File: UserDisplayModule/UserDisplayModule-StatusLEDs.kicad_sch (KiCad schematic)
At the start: 15 parts, among them U1 74HC595

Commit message: doubled LEDs + started PCB
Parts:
- removed D20: SYSTEM FAIL, symbol Device:LED
- removed D21: COL2, symbol Device:LED
- removed D23: COL1, symbol Device:LED
- removed D4: SYSTEM WARN, symbol Device:LED
- added D10, D43, D45: BAT3, LED_SMD:LED_0805_2012Metric, symbol Device:LED
- added D2: MAINS, LED_SMD:LED_0805_2012Metric, symbol Device:LED
- added D42: COL2, LED_SMD:LED_0805_2012Metric, symbol Device:LED
- added D44: COL1, LED_SMD:LED_0805_2012Metric, symbol Device:LED
- added D5: BATTERY, LED_SMD:LED_0805_2012Metric, symbol Device:LED
- added D6: BAT7, LED_SMD:LED_0805_2012Metric, symbol Device:LED
- added D7: SYS WARN, LED_SMD:LED_0805_2012Metric, symbol Device:LED
- added D8: BAT5, LED_SMD:LED_0805_2012Metric, symbol Device:LED
- added D9: SYS FAIL, LED_SMD:LED_0805_2012Metric, symbol Device:LED
- D1: footprint (none) -> LED_SMD:LED_0805_2012Metric
- D3: renamed from D2; footprint (none) -> LED_SMD:LED_0805_2012Metric
- D4: renamed from D3; footprint (none) -> LED_SMD:LED_0805_2012Metric
- R1, R2, R20, R21, R23, R3, R4: footprint (none) -> Resistor_SMD:R_0805_2012Metric
- U1: footprint (none) -> ImportedFootprints:CD74HC595E
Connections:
- net GND: now also D10.1 (K), D2.1 (K), D43.1 (K), D45.1 (K), D6.1 (K), D8.1 (K); no longer D1.1 (K), D3.1 (K)
- net at R21.2: now also D42.2 (A)
- net at R23.2: now also D44.2 (A)
- net at R3.2: now also D5.2 (A); no longer D4.2 (A)
- net at R20.2: now also D9.2 (A)
- net at R4.2: now also D7.2 (A)
- new net: D42.1 (K), D43.2 (A)
- new net: D44.1 (K), D45.2 (A)
- new net: D7.1 (K), D8.2 (A)
- new net: D1.1 (K), D2.2 (A)
- new net: D3.1 (K), D4.2 (A)
- new net: D10.2 (A), D9.1 (K)
- new net: D5.1 (K), D6.2 (A)
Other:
- moved on the sheet: D4, R20, R21, R23

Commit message: started routing (help)
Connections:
- net at R23.1: now also U1.6 (QG); no longer U1.1 (QB)
- net at R1.1: now also U1.5 (QF); no longer U1.7 (QH)
- net at R3.1: now also U1.3 (QD); no longer U1.5 (QF)
- net at R21.1: now also U1.7 (QH); no longer U1.2 (QC)
- net at R20.1: now also U1.1 (QB); no longer U1.3 (QD)
- net at R2.1: now also U1.4 (QE); no longer U1.6 (QG)
- net at R4.1: now also U1.2 (QC); no longer U1.4 (QE)
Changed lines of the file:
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@@
-	(wire
-		(pts
-			(xy 100.33 83.82) (xy 157.48 83.82)
-		)
-		(stroke
-			(width 0)
-			(type default)
-		)
-	)
 	(wire
 		(pts
@@
 	(wire
 		(pts
+			(xy 100.33 88.9) (xy 200.66 88.9)
+		)
+		(stroke
+			(width 0)
+			(type default)
+		)
+	)
+	(wire
+		(pts
+			(xy 100.33 78.74) (xy 157.48 78.74)
+		)
+		(stroke
+			(width 0)
+			(type default)
+		)
+	)
+	(wire
+		(pts
 			(xy 119.38 119.38) (xy 132.08 119.38)
 		)
@@
 	(wire
 		(pts
+			(xy 100.33 76.2) (xy 170.18 76.2)
+		)
+		(stroke
+			(width 0)
+			(type default)
+		)
+	)
+	(wire
+		(pts
 			(xy 77.47 86.36) (xy 80.01 86.36)
 		)
@@
 	(wire
 		(pts
-			(xy 157.48 83.82) (xy 157.48 93.98)
-		)
-		(stroke
-			(width 0)
-			(type default)
-		)
-	)
-	(wire
-		(pts
-			(xy 100.33 76.2) (xy 200.66 76.2)
+			(xy 100.33 91.44) (xy 187.96 91.44)
 		)
 		(stroke
@@
 	(wire
 		(pts
-			(xy 100.33 81.28) (xy 170.18 81.28)
-		)
-		(stroke
-			(width 0)
-			(type default)
-		)
-	)
-	(wire
-		(pts
-			(xy 144.78 86.36) (xy 144.78 93.98)
-		)
-		(stroke
-			(width 0)
-			(type default)
-		)
-	)
-	(wire
-		(pts
-			(xy 119.38 91.44) (xy 119.38 93.98)
+			(xy 132.08 83.82) (xy 132.08 93.98)
+		)
+		(stroke
+			(width 0)
+			(type default)
+		)
+	)
+	(wire
+		(pts
+			(xy 187.96 91.44) (xy 187.96 93.98)
 		)
 		(stroke
@@
 	(wire
 		(pts
-			(xy 100.33 86.36) (xy 144.78 86.36)
-		)
-		(stroke
-			(width 0)
-			(type default)
-		)
-	)
-	(wire
-		(pts
 			(xy 157.48 119.38) (xy 170.18 119.38)
 		)
@@
 	(wire
 		(pts
-			(xy 100.33 78.74) (xy 187.96 78.74)
-		)
-		(stroke
-			(width 0)
-			(type default)
-		)
-	)
-	(wire
-		(pts
 			(xy 100.33 96.52) (xy 101.6 96.52)
 		)
@@
 	(wire
 		(pts
+			(xy 144.78 81.28) (xy 144.78 93.98)
+		)
+		(stroke
+			(width 0)
+			(type default)
+		)
+	)
+	(wire
+		(pts
 			(xy 77.47 73.66) (xy 80.01 73.66)
 		)
@@
 	(wire
 		(pts
-			(xy 170.18 81.28) (xy 170.18 93.98)
+			(xy 119.38 86.36) (xy 119.38 93.98)
 		)
 		(stroke
@@
 	(wire
 		(pts
-			(xy 100.33 91.44) (xy 119.38 91.44)
-		)
-		(stroke
-			(width 0)
-			(type default)
-		)
-	)
-	(wire
-		(pts
 			(xy 77.47 78.74) (xy 80.01 78.74)
 		)
@@
 	(wire
 		(pts
-			(xy 132.08 88.9) (xy 132.08 93.98)
-		)
-		(stroke
-			(width 0)
-			(type default)
-		)
-	)
-	(wire
-		(pts
-			(xy 187.96 78.74) (xy 187.96 93.98)
-		)
-		(stroke
-			(width 0)
-			(type default)
-		)
-	)
-	(wire
-		(pts
-			(xy 200.66 76.2) (xy 200.66 93.98)
+			(xy 100.33 81.28) (xy 144.78 81.28)
+		)
+		(stroke
+			(width 0)
+			(type default)
+		)
+	)
+	(wire
+		(pts
+			(xy 100.33 83.82) (xy 132.08 83.82)
+		)
+		(stroke
+			(width 0)
+			(type default)
+		)
+	)
+	(wire
+		(pts
+			(xy 157.48 78.74) (xy 157.48 93.98)
+		)
+		(stroke
+			(width 0)
+			(type default)
+		)
+	)
+	(wire
+		(pts
+			(xy 200.66 88.9) (xy 200.66 93.98)
 		)
 		(stroke
@@
 	(wire
 		(pts
-			(xy 100.33 88.9) (xy 132.08 88.9)
+			(xy 170.18 76.2) (xy 170.18 93.98)
 		)
 		(stroke
@@
 		)
 	)
+	(wire
+		(pts
+			(xy 100.33 86.36) (xy 119.38 86.36)
+		)
+		(stroke
+			(width 0)
+			(type default)
+		)
+	)
 	(rectangle
-		(start 113.03 93.98)
+		(start 113.03 92.71)
 		(end 179.07 125.73)
 		(stroke

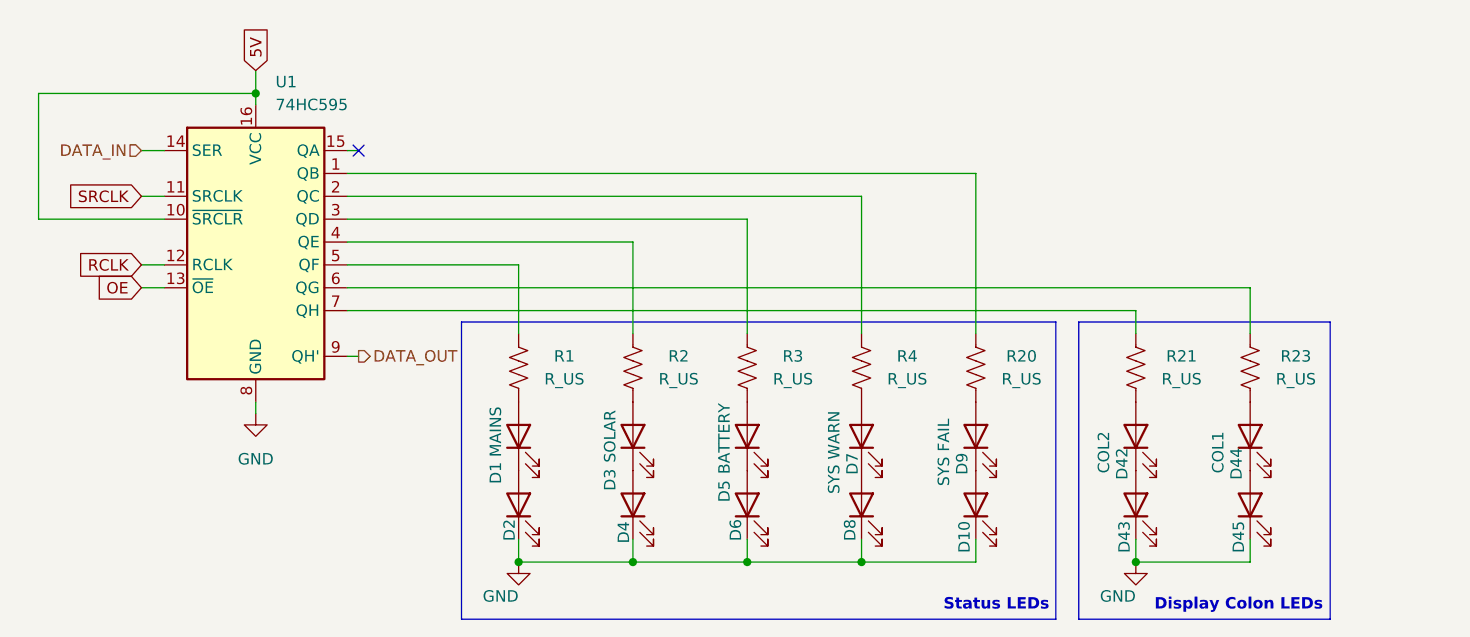
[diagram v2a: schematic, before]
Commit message: finished routing pcb (minus ground pour)
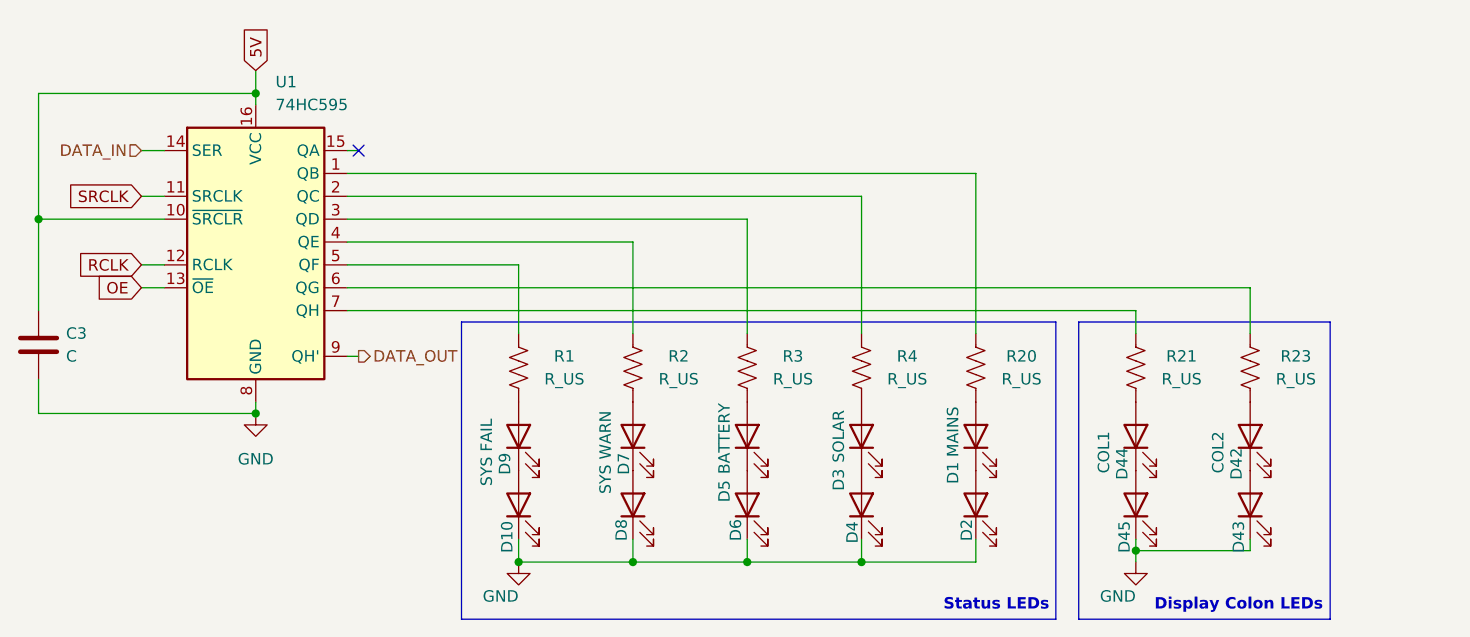
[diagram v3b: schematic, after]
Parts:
- added C3: C, Capacitor_SMD:C_0805_2012Metric, symbol Device:C
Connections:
- net 5V: now also C3.1
- net GND: now also C3.2
- net at R23.2: now also D42.2 (A); no longer D44.2 (A)
- net at R1.2: now also D9.2 (A); no longer D1.2 (A)
- net at R21.2: now also D44.2 (A); no longer D42.2 (A)
- net at R20.2: now also D1.2 (A); no longer D9.2 (A)
- net at R2.2: now also D7.2 (A); no longer D3.2 (A)
- net at R4.2: now also D3.2 (A); no longer D7.2 (A)
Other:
- moved on the sheet: D1, D10, D2, D3, D4, D42, D43, D44, D45, D7, D8, D9

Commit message: added 3d models, fixed footprints, finished routing
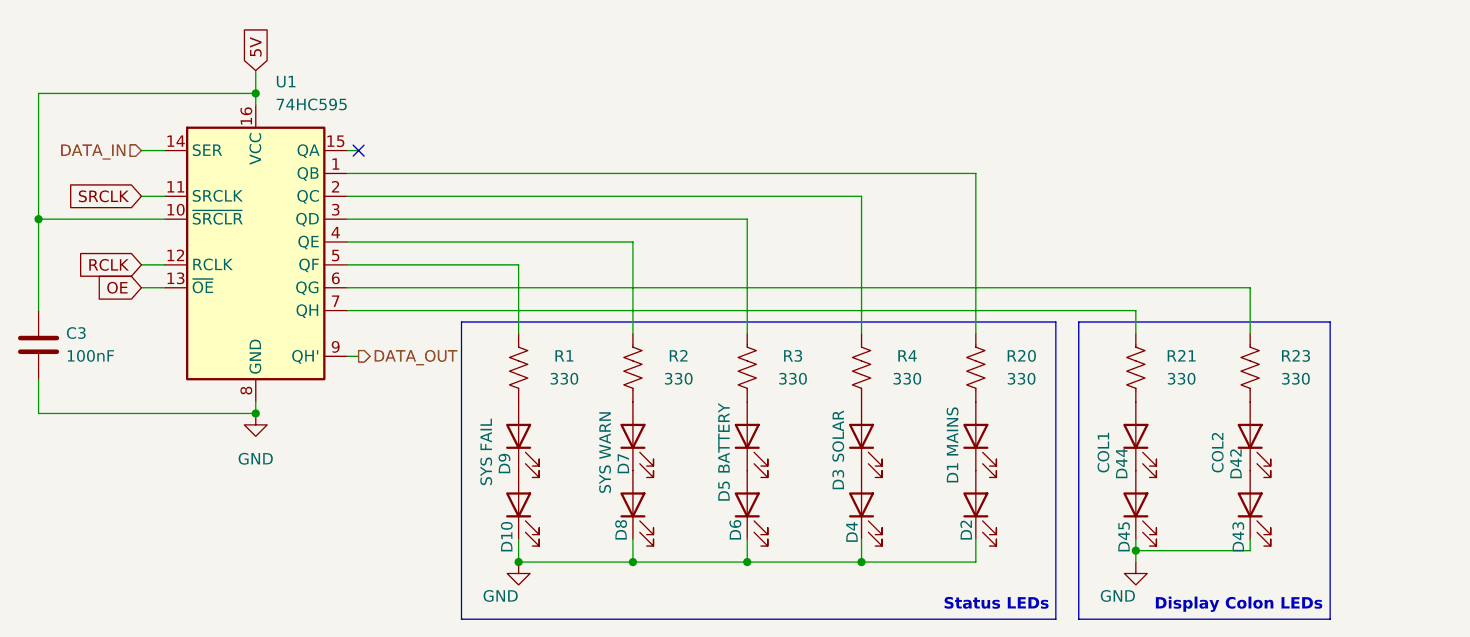
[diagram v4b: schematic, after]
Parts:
- C3: value C -> 100nF
- R1, R2, R20, R21, R23, R3, R4: value R_US -> 330
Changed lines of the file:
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@@
 			)
 		)
-		(property "Value" "R_US"
+		(property "Value" "330"
 			(at 205.74 99.06 0)
 			(effects
@@
 			)
 		)
-		(property "Value" "R_US"
+		(property "Value" "330"
 			(at 124.46 99.06 0)
 			(effects
@@
 			)
 		)
-		(property "Value" "R_US"
+		(property "Value" "330"
 			(at 149.86 99.06 0)
 			(effects
@@
 			)
 		)
-		(property "Value" "R_US"
+		(property "Value" "330"
 			(at 193.04 99.06 0)
 			(effects
@@
 			)
 		)
-		(property "Value" "R_US"
+		(property "Value" "330"
 			(at 175.26 99.06 0)
 			(effects
@@
 			)
 		)
-		(property "Value" "R_US"
+		(property "Value" "330"
 			(at 137.16 99.06 0)
 			(effects
@@
 			)
 		)
-		(property "Value" "R_US"
+		(property "Value" "330"
 			(at 162.56 99.06 0)
 			(effects
@@
 			)
 		)
-		(property "Value" "C"
+		(property "Value" "100nF"
 			(at 69.088 96.52 0)
 			(effects

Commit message: added digikey pns
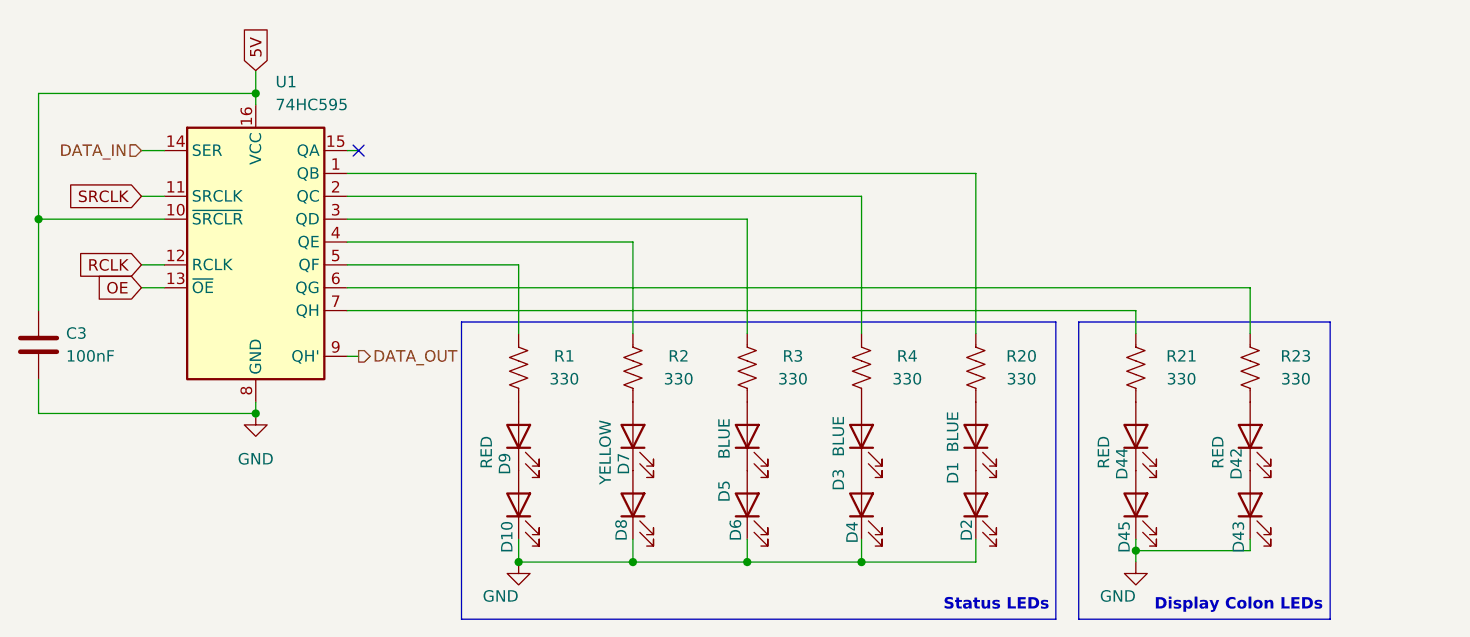
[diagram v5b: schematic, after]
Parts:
- D1, D2: value MAINS -> BLUE; Digikey PN (none) -> 732-4982-1-ND
- D10, D43, D45: value BAT3 -> RED; Digikey PN (none) -> 732-4984-1-ND
- D3: value SOLAR -> BLUE; Digikey PN (none) -> 732-4982-1-ND
- D4, D5: value BATTERY -> BLUE; Digikey PN (none) -> 732-4982-1-ND
- D42: value COL2 -> RED; Digikey PN (none) -> 732-4984-1-ND
- D44: value COL1 -> RED; Digikey PN (none) -> 732-4984-1-ND
- D6: value BAT7 -> BLUE; Digikey PN (none) -> 732-4982-1-ND
- D7: value SYS WARN -> YELLOW; Digikey PN (none) -> 732-4987-1-ND
- D8: value BAT5 -> YELLOW; Digikey PN (none) -> 732-4987-1-ND
- D9: value SYS FAIL -> RED; Digikey PN (none) -> 732-4984-1-ND
- U1: Digikey PN (none) -> 296-1600-5-ND
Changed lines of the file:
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@@
+			)
+		)
+		(property "Digikey PN" ""
+			(at 200.66 97.79 0)
+			(effects
+				(font
+					(size 1.27 1.27)
+				)
+				(hide yes)
 			)
 		)
@@
 		)
 		(property "Description" "Resistor, US symbol"
+			(at 119.38 97.79 0)
+			(effects
+				(font
+					(size 1.27 1.27)
+				)
+				(hide yes)
+			)
+		)
+		(property "Digikey PN" ""
 			(at 119.38 97.79 0)
 			(effects
@@
 			)
 		)
+		(property "Digikey PN" ""
+			(at 144.78 97.79 0)
+			(effects
+				(font
+					(size 1.27 1.27)
+				)
+				(hide yes)
+			)
+		)
 		(pin "1"
 		)
@@
 			)
 		)
-		(property "Value" "BAT3"
+		(property "Value" "RED"
 			(at 206.6925 116.205 90)
 			(effects
@@
 			)
 		)
+		(property "Digikey PN" "732-4984-1-ND"
+			(at 200.66 113.03 0)
+			(effects
+				(font
+					(size 1.27 1.27)
+				)
+				(hide yes)
+			)
+		)
 		(pin "1"
 		)
@@
 			)
 		)
-		(property "Value" "COL1"
+		(property "Value" "RED"
 			(at 184.404 107.188 0)
 			(effects
@@
 			)
 		)
+		(property "Digikey PN" "732-4984-1-ND"
+			(at 187.96 105.41 0)
+			(effects
+				(font
+					(size 1.27 1.27)
+				)
+				(hide yes)
+			)
+		)
 		(pin "1"
 		)
@@
 			)
 		)
+		(property "Digikey PN" ""
+			(at 187.96 97.79 0)
+			(effects
+				(font
+					(size 1.27 1.27)
+				)
+				(hide yes)
+			)
+		)
 		(pin "1"
 		)
@@
 			)
 		)
-		(property "Value" "BAT5"
+		(property "Value" "YELLOW"
 			(at 138.1125 116.205 90)
 			(effects
@@
 			)
 		)
+		(property "Digikey PN" "732-4987-1-ND"
+			(at 132.08 113.03 0)
+			(effects
+				(font
+					(size 1.27 1.27)
+				)
+				(hide yes)
+			)
+		)
 		(pin "1"
 		)
@@
 			)
 		)
+		(property "Digikey PN" ""
+			(at 170.18 97.79 0)
+			(effects
+				(font
+					(size 1.27 1.27)
+				)
+				(hide yes)
+			)
+		)
 		(pin "1"
 		)
@@
 			)
 		)
-		(property "Value" "MAINS"
+		(property "Value" "BLUE"
 			(at 173.736 110.998 0)
 			(effects
@@
 			)
 		)
+		(property "Digikey PN" "732-4982-1-ND"
+			(at 170.18 113.03 0)
+			(effects
+				(font
+					(size 1.27 1.27)
+				)
+				(hide yes)
+			)
+		)
 		(pin "1"
 		)
@@
 			)
 		)
+		(property "Digikey PN" ""
+			(at 132.08 97.79 0)
+			(effects
+				(font
+					(size 1.27 1.27)
+				)
+				(hide yes)
+			)
+		)
 		(pin "1"
 		)
@@
 			)
 		)
-		(property "Value" "BATTERY"
+		(property "Value" "BLUE"
 			(at 163.83 114.3 90)
 			(effects
@@
 			)
 		)
+		(property "Digikey PN" "732-4982-1-ND"
+			(at 157.48 113.03 0)
+			(effects
+				(font
+					(size 1.27 1.27)
+				)
+				(hide yes)
+			)
+		)
 		(pin "1"
 		)
@@
 			)
 		)
+		(property "Digikey PN" ""
+			(at 157.48 97.79 0)
+			(effects
+				(font
+					(size 1.27 1.27)
+				)
+				(hide yes)
+			)
+		)
 		(pin "1"
 		)
@@
 			)
 		)
-		(property "Value" "SYS FAIL"
+		(property "Value" "RED"
 			(at 115.824 107.188 0)
 			(effects
@@
 			)
 		)
+		(property "Digikey PN" "732-4984-1-ND"
+			(at 119.38 105.41 0)
+			(effects
+				(font
+					(size 1.27 1.27)
+				)
+				(hide yes)
+			)
+		)
 		(pin "1"
 		)
@@
 			)
 		)
-		(property "Value" "SOLAR"
+		(property "Value" "BLUE"
 			(at 154.94 105.41 0)
 			(effects
@@
 			)
 		)
+		(property "Digikey PN" "732-4982-1-ND"
+			(at 157.48 105.41 0)
+			(effects
+				(font
+					(size 1.27 1.27)
+				)
+				(hide yes)
+			)
+		)
 		(pin "1"
 		)
@@
 			)
 		)
-		(property "Value" "MAINS"
+		(property "Value" "BLUE"
 			(at 167.64 104.902 0)
 			(effects
@@
 			)
 		)
+		(property "Digikey PN" "732-4982-1-ND"
+			(at 170.18 105.41 0)
+			(effects
+				(font
+					(size 1.27 1.27)
+				)
+				(hide yes)
+			)
+		)
 		(pin "1"
 		)
@@
 			)
 		)
-		(property "Value" "BATTERY"
+		(property "Value" "BLUE"
 			(at 142.24 105.664 0)
 			(effects
@@
 			)
 		)
+		(property "Digikey PN" "732-4982-1-ND"
+			(at 144.78 105.41 0)
+			(effects
+				(font
+					(size 1.27 1.27)
+				)
+				(hide yes)
+			)
+		)
 		(pin "1"
 		)
@@
 			)
 		)
-		(property "Value" "SYS WARN"
+		(property "Value" "YELLOW"
 			(at 129.032 107.188 0)
 			(effects
@@
 		)
 		(property "Description" "Light emitting diode"
+			(at 132.08 105.41 0)
+			(effects
+				(font
+					(size 1.27 1.27)
+				)
+				(hide yes)
+			)
+		)
+		(property "Digikey PN" "732-4987-1-ND"
 			(at 132.08 105.41 0)
 			(effects
@@
 			)
 		)
+		(property "Digikey PN" "296-1600-5-ND"
+			(at 90.17 83.82 0)
+			(effects
+				(font
+					(size 1.27 1.27)
+				)
+				(hide yes)
+			)
+		)
 		(pin "9"
 		)
@@
 			)
 		)
-		(property "Value" "COL2"
+		(property "Value" "RED"
 			(at 197.104 107.188 0)
 			(effects
@@
 			)
 		)
+		(property "Digikey PN" "732-4984-1-ND"
+			(at 200.66 105.41 0)
+			(effects
+				(font
+					(size 1.27 1.27)
+				)
+				(hide yes)
+			)
+		)
 		(pin "1"
 		)
@@
 			)
 		)
-		(property "Value" "BAT3"
+		(property "Value" "RED"
 			(at 125.4125 116.205 90)
 			(effects
@@
 			)
 		)
+		(property "Digikey PN" "732-4984-1-ND"
+			(at 119.38 113.03 0)
+			(effects
+				(font
+					(size 1.27 1.27)
+				)
+				(hide yes)
+			)
+		)
 		(pin "1"
 		)
@@
 			)
 		)
+		(property "Digikey PN" ""
+			(at 66.04 95.25 0)
+			(effects
+				(font
+					(size 1.27 1.27)
+				)
+				(hide yes)
+			)
+		)
 		(pin "2"
 		)
@@
 			)
 		)
-		(property "Value" "BAT7"
+		(property "Value" "BLUE"
 			(at 150.8125 116.205 90)
 			(effects
@@
 			)
 		)
+		(property "Digikey PN" "732-4982-1-ND"
+			(at 144.78 113.03 0)
+			(effects
+				(font
+					(size 1.27 1.27)
+				)
+				(hide yes)
+			)
+		)
 		(pin "1"
 		)
@@
 			)
 		)
-		(property "Value" "BAT3"
+		(property "Value" "RED"
 			(at 193.9925 116.205 90)
 			(effects
@@
 			(at 187.96 113.03 0)
 			(effects
+				(font
+					(size 1.27 1.27)
+				)
+				(hide yes)
+			)
+		)
+		(property "Digikey PN" "732-4984-1-ND"
+			(at 187.96 113.03 0)
+			(effects
